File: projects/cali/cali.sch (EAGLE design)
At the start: 28 parts, among them T1 IRLML2502, T2 IRLML2502, T3 2N7002E, T4 IRLML2502

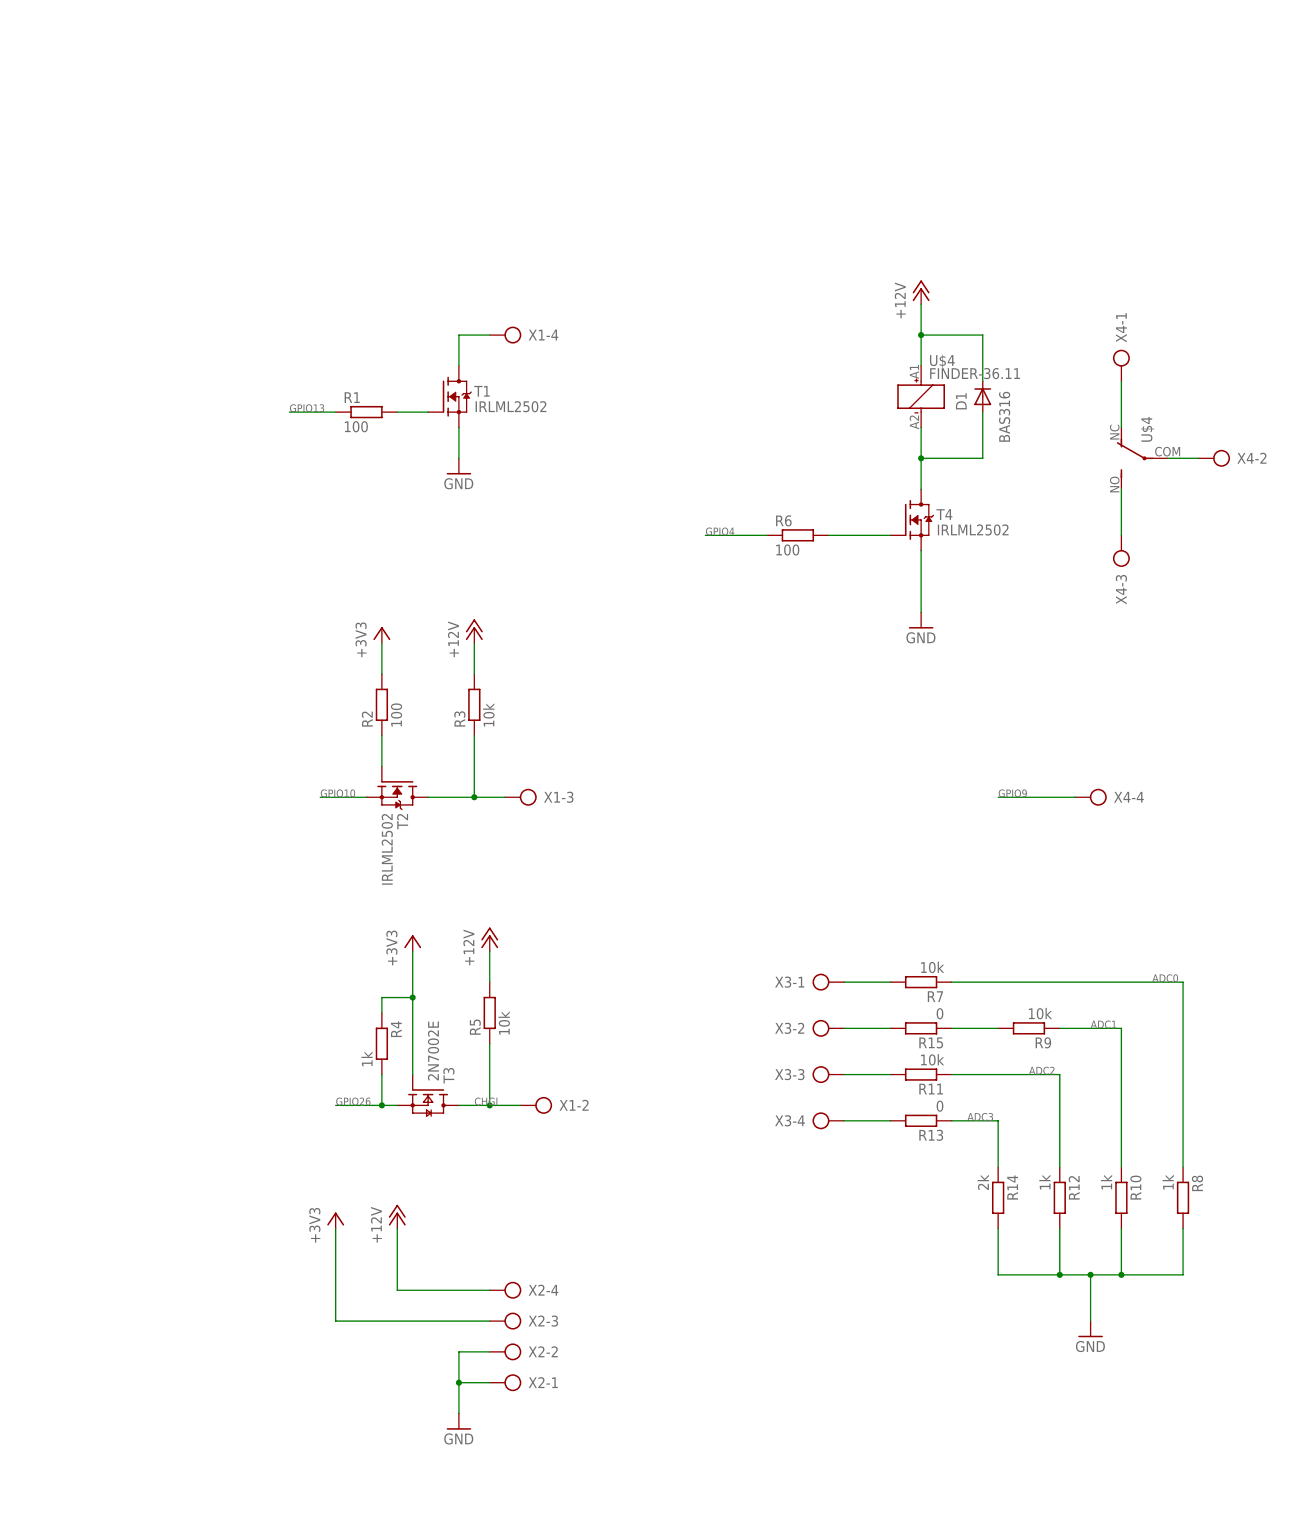
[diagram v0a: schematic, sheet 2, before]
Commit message: Caliboard 1.2
- Fan output now has a PP stage
- Temp-sensor 4k7 pull up
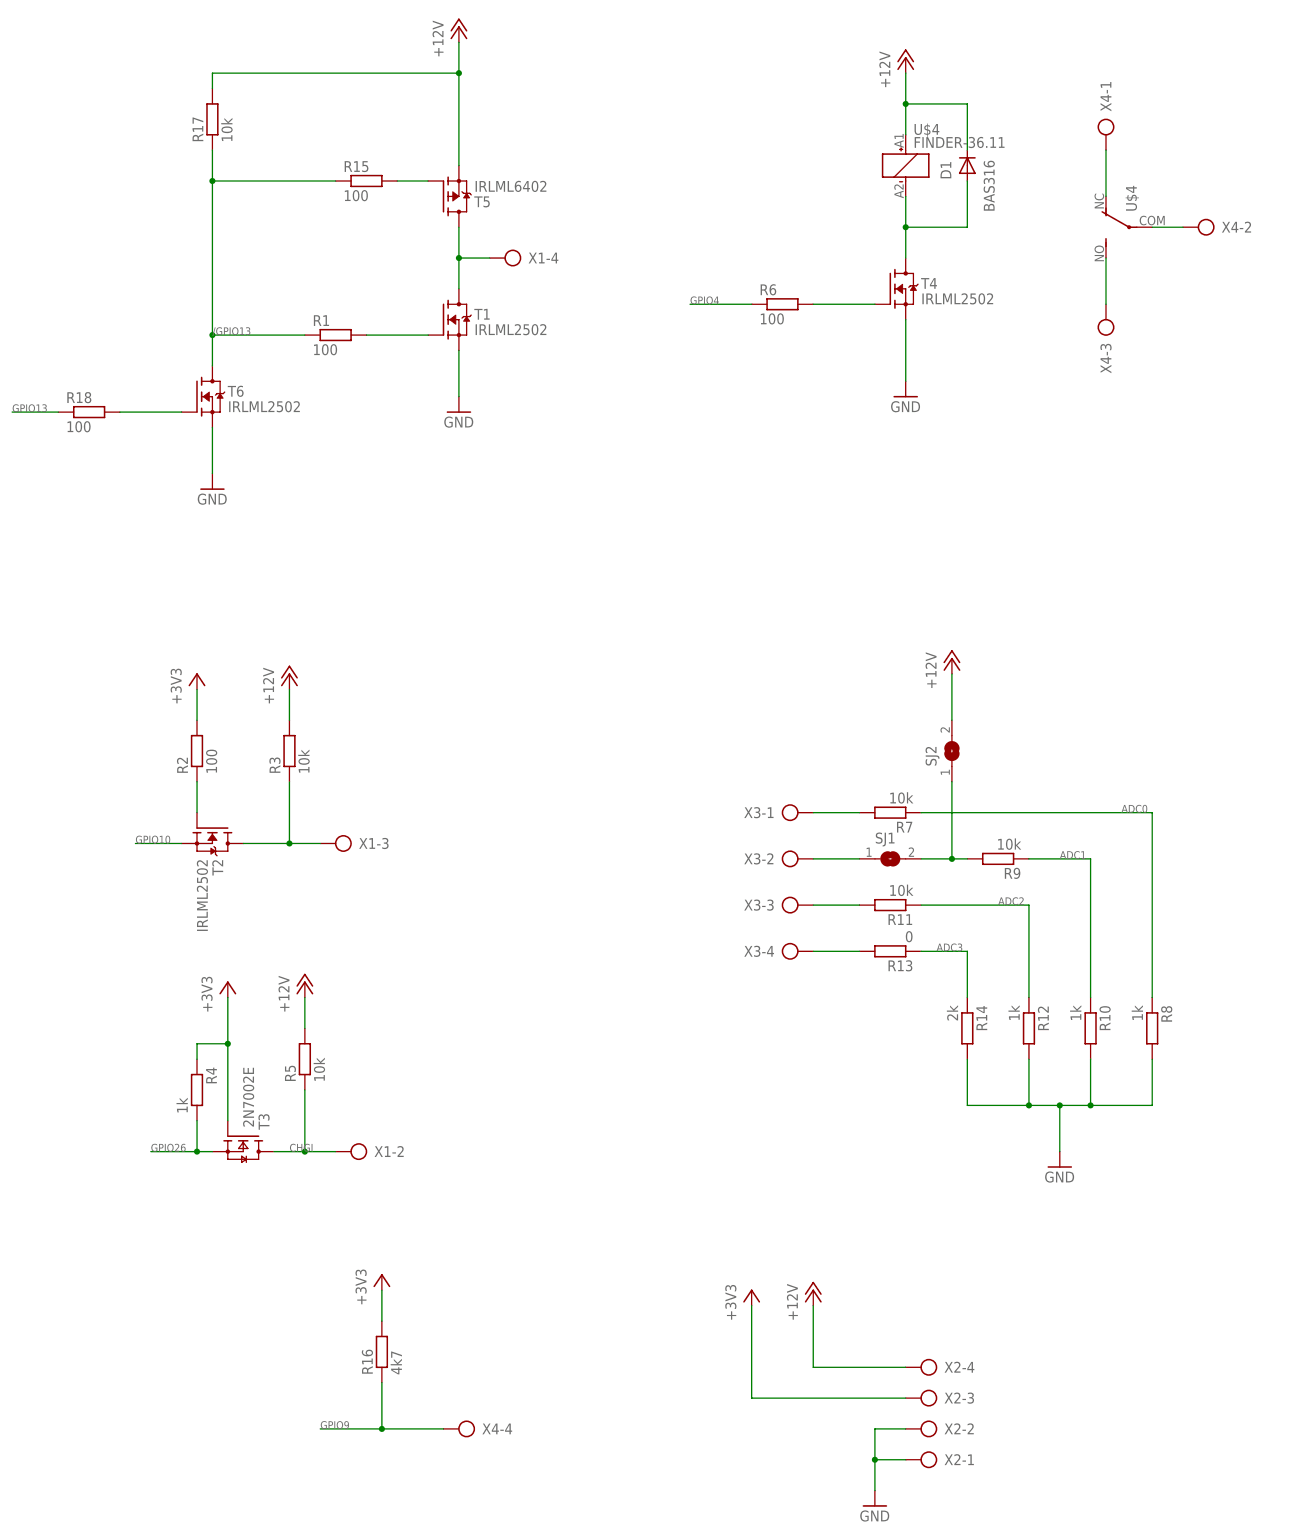
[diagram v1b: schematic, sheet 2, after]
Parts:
- added R16: 4k7, rcl:R-EU_R1206
- added R17: 10k, rcl:R-EU_R1206
- added R18: 100, rcl:R-EU_R1206
- added SJ1, SJ2: (no value), jumper:SJ
- added T5: IRLML6402, we-transistor:MOSFET-P-SOT23
- added T6: IRLML2502, we-transistor:MOSFET-N-SOT23
- R15: value 0 -> 100
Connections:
- removed net N$9: R15.2, X3-2.KL
- new net /GPIO13: R1.1, R15.1, R17.1, T6.D
- new net N$12: R18.2, T6.G
- new net N$8: R15.2, T5.G
- new net V_BAT: SJ1.1, X3-2.KL
- net +12V: now also R17.2, SJ2.2, T5.S
- net +3V3: now also R16.2
- net GND: now also T6.S
- net GPIO13: now also R18.1; no longer R1.1
- net GPIO9: now also R16.1
- net N$13: now also SJ1.2, SJ2.1; no longer R15.1
- net N$2: now also T5.D
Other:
- note added: "Cali Board v1.2"
- note added: "Tempsensor"
- note removed: "Cali Board v1.1"
- moved on the sheet: D1, R1, R10, R11, R12, R13, R14, R15, R2, R3, R4, R5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

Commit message: Caliboard 1.4
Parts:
- removed D1: BAS316, nxp_60:BAS316
- removed R15, R18, R2, R6: 100, rcl:R-EU_R1206
- removed R17, R3, R5: 10k, rcl:R-EU_R1206
- removed T1, T2, T4, T6: IRLML2502, we-transistor:MOSFET-N-SOT23
- removed T3: 2N7002E, nxp_60:2N7002E
- removed T5: IRLML6402, we-transistor:MOSFET-P-SOT23
- added D2: BZX384-3V3, nxp_60:BZX84J
- added IC1: L293DD, st-microelectronics:L293DD
- R1: value 100 -> DNP
- R4: value 1k -> 10k
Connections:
- removed net /GPIO13: R1.1, R15.1, R17.1, T6.D
- removed net CHGI: R5.1, T3.D, X1-2.KL
- removed net GPIO4: R6.1, U$2.GPIO4/GCKL
- removed net N$1: D1.A, T4.D, U$4G$1.-
- removed net N$10: R2.1, T2.G
- removed net N$11: R3.1, T2.D, X1-3.KL
- removed net N$12: R18.2, T6.G
- removed net N$4: R6.2, T4.G
- removed net N$8: R15.2, T5.G
- new net DRVOUT3: IC1.OUT3, U$4G$1.+
- new net GPIO5: IC1.IN2, U$2.GPIO5
- new net GPIO6: IC1.IN3, U$2.GPIO6
- new net N$9: R1.1, R4.2, X1-2.KL
- net +12V: now also IC1.VS, IC1.VSS; no longer D1.K, R17.2, R3.2, R5.2, T5.S, U$4G$1.+
- net +3V3: now also IC1.EN1, IC1.EN2; no longer R2.2, R4.1, T3.G
- net GND: now also D2.A, IC1.GND@1, IC1.GND@2, IC1.GND@3, IC1.GND@4, IC1.GND@5, IC1.GND@6, IC1.GND@7, IC1.GND@8, IC1.IN4, R1.2, U$4G$1.-; no longer T1.S, T4.S, T6.S
- net GPIO10: no longer T2.S
- net GPIO13: now also IC1.IN1; no longer R18.1
- net GPIO26: now also D2.C, R4.1; no longer R4.2, T3.S
- net N$2: now also IC1.OUT1; no longer T1.D, T5.D
- net N$6: now also IC1.OUT2, X1-3.KL; no longer R1.2, T1.G
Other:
- note added: "Cali Board v1.3"
- note added: "Treiber"
- note removed: "Cali Board v1.2"
- note removed: "Lüfter"
- moved on the sheet: R1, R4, X1-2, X1-3, X1-4

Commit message: Add additional 12V input
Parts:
- added D1: BZX384-3V3, nxp_60:BZX84J
- added R2: 10k, rcl:R-EU_R1206
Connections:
- new net N$1: R2.2, X1-1.KL
- net GND: now also D1.A
- net GPIO19: now also D1.C, R2.1
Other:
- note added: "Cali Board v1.5"
- note removed: "Cali Board v1.3"
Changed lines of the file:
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@@
 <?xml version="1.0" encoding="utf-8"?>
 <!DOCTYPE eagle SYSTEM "eagle.dtd">
-<eagle version="9.5.0">
+<eagle version="9.6.2">
 <drawing>
 <settings>
@@
 <part name="GND10" library="supply1" deviceset="GND" device=""/>
 <part name="+3V8" library="supply1" deviceset="+3V3" device=""/>
+<part name="R2" library="rcl" deviceset="R-EU_" device="R1206" value="10k"/>
+<part name="D1" library="nxp_60" deviceset="BZX84J" device="" value="BZX384-3V3"/>
+<part name="GND7" library="supply1" deviceset="GND" device=""/>
 </parts>
 <sheets>
@@
 <wire x1="139.7" y1="99.06" x2="0" y2="99.06" width="0.1524" layer="254"/>
 <wire x1="0" y1="99.06" x2="0" y2="0" width="0.1524" layer="254"/>
-<text x="111.76" y="5.08" size="2.54" layer="254">Cali Board v1.3</text>
+<text x="111.76" y="5.08" size="2.54" layer="254">Cali Board v1.5</text>
 </plain>
 <instances>
@@
 <attribute name="VALUE" x="-55.88" y="170.18" size="1.778" layer="96" rot="R90"/>
 </instance>
+<instance part="X1" gate="-1" x="-63.5" y="55.88" smashed="yes">
+<attribute name="NAME" x="-64.77" y="56.769" size="1.778" layer="95" rot="R180"/>
+</instance>
+<instance part="R2" gate="G$1" x="-45.72" y="55.88" smashed="yes" rot="R180">
+<attribute name="NAME" x="-41.91" y="54.3814" size="1.778" layer="95" rot="R180"/>
+<attribute name="VALUE" x="-41.91" y="59.182" size="1.778" layer="96" rot="R180"/>
+</instance>
+<instance part="D1" gate="G$1" x="-35.56" y="48.26" smashed="yes" rot="R90">
+<attribute name="NAME" x="-37.465" y="46.482" size="1.778" layer="95" font="vector" rot="R90"/>
+<attribute name="VALUE" x="-32.131" y="38.862" size="1.778" layer="96" font="vector" rot="R90"/>
+</instance>
+<instance part="GND7" gate="1" x="-35.56" y="33.02" smashed="yes"/>
 </instances>
 <busses>
@@
 <wire x1="63.5" y1="149.86" x2="63.5" y2="142.24" width="0.1524" layer="91"/>
 </segment>
+<segment>
+<pinref part="GND7" gate="1" pin="GND"/>
+<pinref part="D1" gate="G$1" pin="A"/>
+<wire x1="-35.56" y1="35.56" x2="-35.56" y2="45.72" width="0.1524" layer="91"/>
+</segment>
 </net>
 <net name="+12V" class="0">
@@
 </segment>
 </net>
+<net name="N$1" class="0">
+<segment>
+<pinref part="X1" gate="-1" pin="KL"/>
+<pinref part="R2" gate="G$1" pin="2"/>
+<wire x1="-58.42" y1="55.88" x2="-50.8" y2="55.88" width="0.1524" layer="91"/>
+</segment>
+</net>
+<net name="GPIO19" class="0">
+<segment>
+<pinref part="R2" gate="G$1" pin="1"/>
+<pinref part="D1" gate="G$1" pin="C"/>
+<wire x1="-40.64" y1="55.88" x2="-35.56" y2="55.88" width="0.1524" layer="91"/>
+<wire x1="-35.56" y1="55.88" x2="-35.56" y2="50.8" width="0.1524" layer="91"/>
+<wire x1="-35.56" y1="55.88" x2="-17.78" y2="55.88" width="0.1524" layer="91"/>
+<junction x="-35.56" y="55.88"/>
+<label x="-22.86" y="55.88" size="1.27" layer="95"/>
+</segment>
+</net>
